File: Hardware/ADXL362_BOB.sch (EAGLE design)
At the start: 9 parts, among them U1 ADXL362

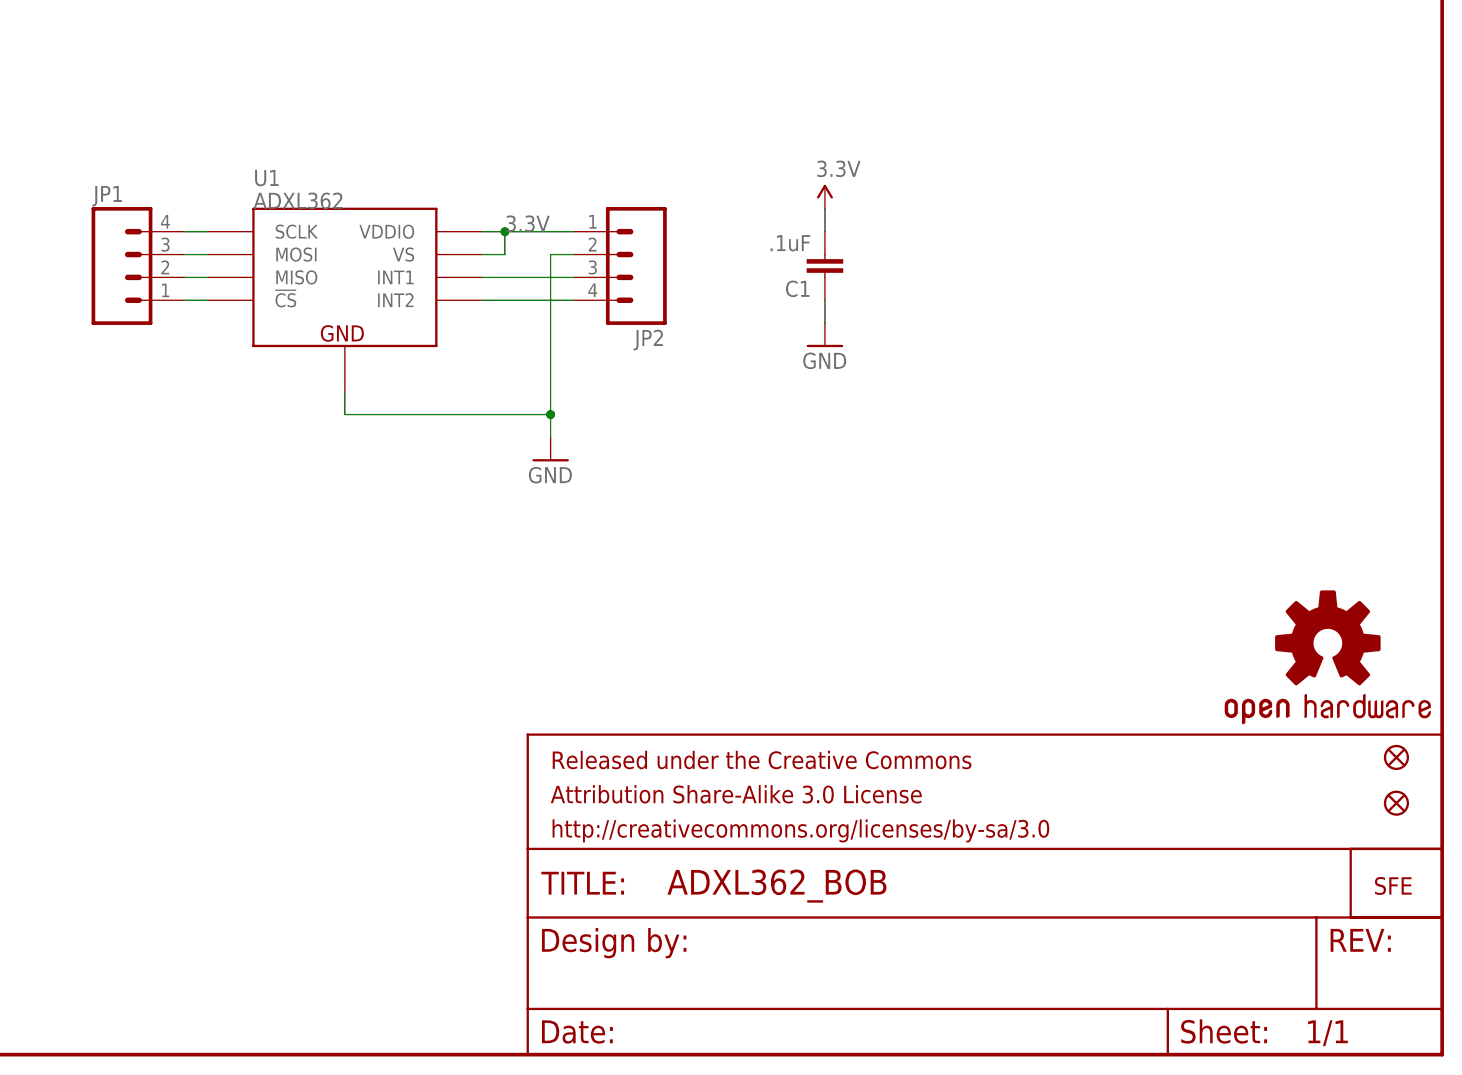
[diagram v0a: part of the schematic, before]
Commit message: Moved to 0603, Traces, 1:1
1:1 on the Adxl362
Minor trace re-route
cap moved to 0603
Sch update
Rev #1 update
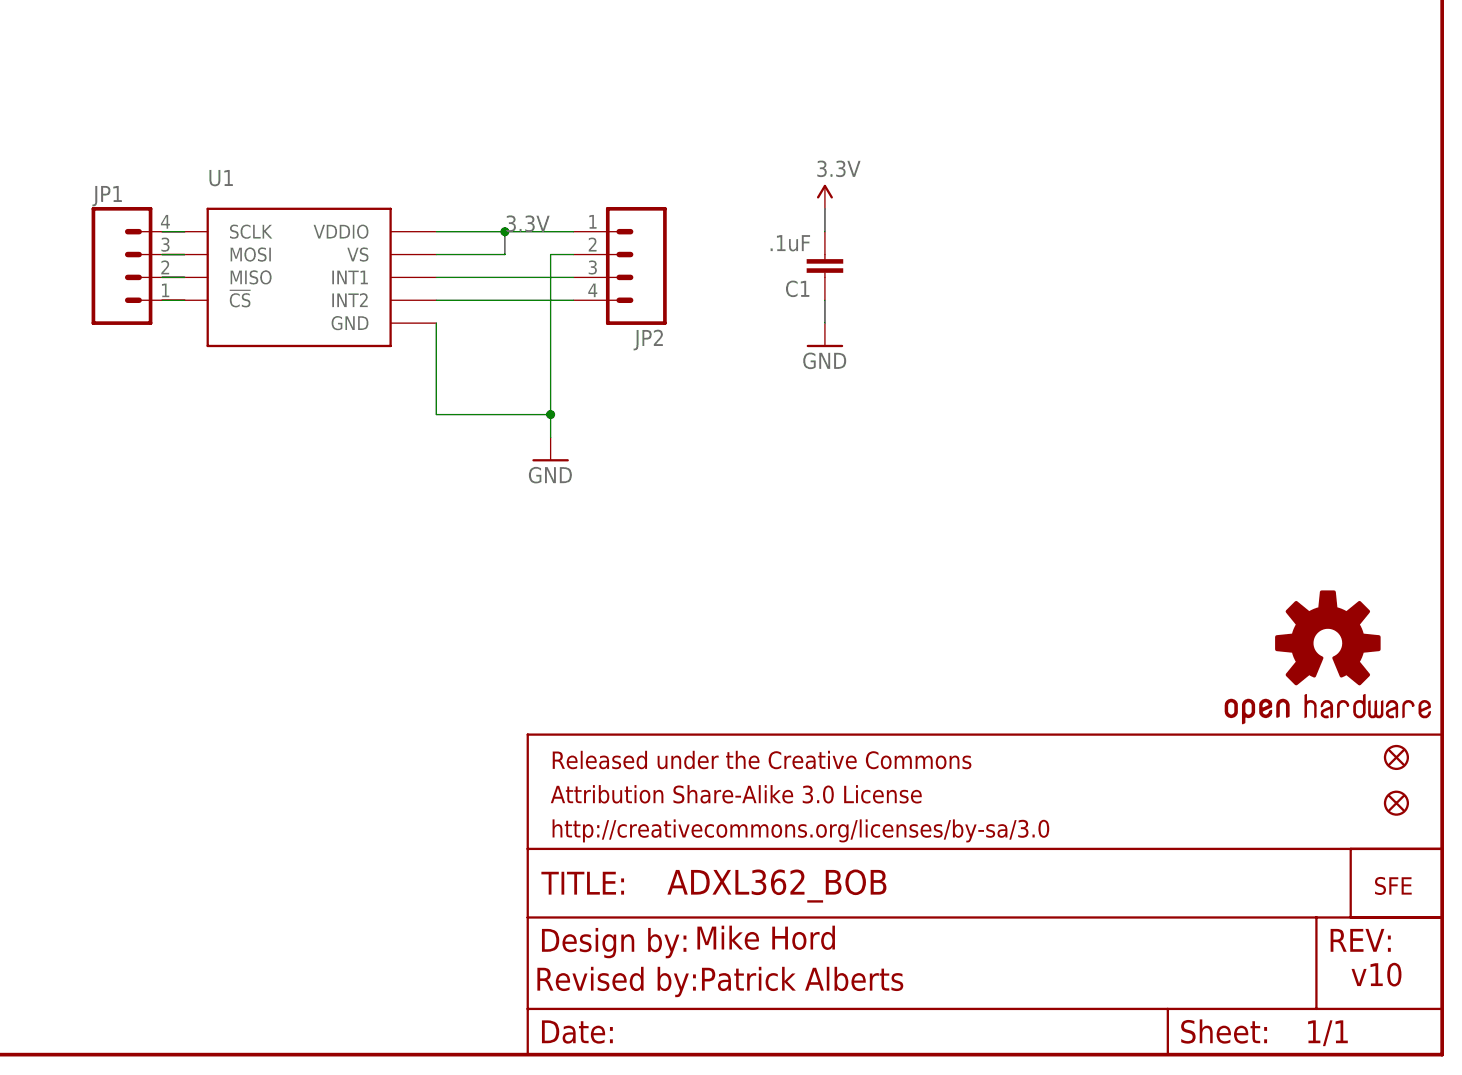
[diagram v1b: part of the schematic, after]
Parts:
- C1: device SparkFun-Passives:CAP0402-CAP -> SparkFun-Capacitors:0.1UF-25V(+80/-20%)(0603)
- U1: value ADXL362 -> (none); device SparkFun-Sensors:ADXL362 -> SparkFun-Sensors:ADXL362ADXL362-1:1
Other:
- note added: "Mike Hord"
- note added: "Revised by:Patrick Alberts"
- note added: "v10"
- moved on the sheet: U1
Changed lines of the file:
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@@
 <?xml version="1.0" encoding="utf-8"?>
 <!DOCTYPE eagle SYSTEM "eagle.dtd">
-<eagle version="6.2">
+<eagle version="6.4">
 <drawing>
 <settings>
@@
 <layer number="106" name="bPlate" color="7" fill="1" visible="no" active="yes"/>
 <layer number="107" name="Crop" color="7" fill="1" visible="no" active="yes"/>
+<layer number="108" name="tplace-old" color="10" fill="1" visible="yes" active="yes"/>
+<layer number="109" name="ref-old" color="11" fill="1" visible="yes" active="yes"/>
 <layer number="116" name="Patch_BOT" color="9" fill="4" visible="no" active="yes"/>
 <layer number="121" name="_tsilk" color="7" fill="1" visible="no" active="yes"/>
@@
 <layer number="144" name="Drill_legend" color="7" fill="1" visible="no" active="yes"/>
 <layer number="151" name="HeatSink" color="7" fill="1" visible="no" active="yes"/>
+<layer number="199" name="Contour" color="7" fill="1" visible="yes" active="yes"/>
 <layer number="200" name="200bmp" color="1" fill="10" visible="no" active="yes"/>
 <layer number="201" name="201bmp" color="2" fill="10" visible="no" active="yes"/>
@@
 </classes>
 <parts>
-<part name="U1" library="SparkFun-Sensors" deviceset="ADXL362" device=""/>
+<part name="U1" library="SparkFun-Sensors" deviceset="ADXL362" device="ADXL362-1:1"/>
 <part name="JP1" library="SparkFun-Connectors" deviceset="M04" device="PTH"/>
 <part name="JP2" library="SparkFun-Connectors" deviceset="M04" device="PTH"/>
-<part name="C1" library="SparkFun-Passives" deviceset="CAP" device="0402-CAP" value=".1uF">
+<part name="C1" library="SparkFun-Capacitors" deviceset="0.1UF-25V(+80/-20%)(0603)" device="" value=".1uF">
 <attribute name="PROD_ID" value="CAP-00810"/>
 </part>
@@
 <sheet>
 <plain>
+<text x="238.76" y="7.62" size="2.54" layer="94">v10</text>
+<text x="165.862" y="11.684" size="2.54" layer="94">Mike Hord</text>
+<text x="148.082" y="7.112" size="2.54" layer="94">Revised by:Patrick Alberts</text>
 </plain>
 <instances>
-<instance part="U1" gate="G$1" x="119.38" y="78.74"/>
+<instance part="U1" gate="G$1" x="121.92" y="86.36"/>
 <instance part="JP1" gate="G$1" x="104.14" y="86.36"/>
 <instance part="JP2" gate="G$1" x="157.48" y="88.9" rot="R180"/>
@@
 <pinref part="JP1" gate="G$1" pin="4"/>
 <pinref part="U1" gate="G$1" pin="SCLK"/>
-<wire x1="109.22" y1="91.44" x2="111.76" y2="91.44" width="0.1524" layer="91"/>
+<wire x1="109.22" y1="91.44" x2="106.68" y2="91.44" width="0.1524" layer="91"/>
 </segment>
 </net>
@@
 <pinref part="U1" gate="G$1" pin="MOSI"/>
 <pinref part="JP1" gate="G$1" pin="3"/>
-<wire x1="111.76" y1="88.9" x2="109.22" y2="88.9" width="0.1524" layer="91"/>
+<wire x1="106.68" y1="88.9" x2="109.22" y2="88.9" width="0.1524" layer="91"/>
 </segment>
 </net>
@@
 <pinref part="JP1" gate="G$1" pin="2"/>
 <pinref part="U1" gate="G$1" pin="MISO"/>
-<wire x1="109.22" y1="86.36" x2="111.76" y2="86.36" width="0.1524" layer="91"/>
+<wire x1="109.22" y1="86.36" x2="106.68" y2="86.36" width="0.1524" layer="91"/>
 </segment>
 </net>
@@
 <pinref part="U1" gate="G$1" pin="!CS"/>
 <pinref part="JP1" gate="G$1" pin="1"/>
-<wire x1="111.76" y1="83.82" x2="109.22" y2="83.82" width="0.1524" layer="91"/>
+<wire x1="106.68" y1="83.82" x2="109.22" y2="83.82" width="0.1524" layer="91"/>
 </segment>
 </net>
@@
 <wire x1="152.4" y1="91.44" x2="144.78" y2="91.44" width="0.1524" layer="91"/>
 <pinref part="U1" gate="G$1" pin="VS"/>
-<wire x1="144.78" y1="91.44" x2="142.24" y2="91.44" width="0.1524" layer="91"/>
-<wire x1="142.24" y1="88.9" x2="144.78" y2="88.9" width="0.1524" layer="91"/>
+<wire x1="144.78" y1="91.44" x2="137.16" y2="91.44" width="0.1524" layer="91"/>
+<wire x1="137.16" y1="88.9" x2="144.78" y2="88.9" width="0.1524" layer="91"/>
 <wire x1="144.78" y1="88.9" x2="144.78" y2="91.44" width="0.1524" layer="91"/>
 <junction x="144.78" y="91.44"/>
@@
 <pinref part="U1" gate="G$1" pin="INT1"/>
 <pinref part="JP2" gate="G$1" pin="3"/>
-<wire x1="152.4" y1="86.36" x2="142.24" y2="86.36" width="0.1524" layer="91"/>
+<wire x1="152.4" y1="86.36" x2="137.16" y2="86.36" width="0.1524" layer="91"/>
 </segment>
 </net>
@@
 <pinref part="U1" gate="G$1" pin="INT2"/>
 <pinref part="JP2" gate="G$1" pin="4"/>
-<wire x1="152.4" y1="83.82" x2="142.24" y2="83.82" width="0.1524" layer="91"/>
+<wire x1="152.4" y1="83.82" x2="137.16" y2="83.82" width="0.1524" layer="91"/>
 </segment>
 </net>
@@
 <segment>
 <pinref part="U1" gate="G$1" pin="GND"/>
-<wire x1="127" y1="73.66" x2="127" y2="71.12" width="0.1524" layer="91"/>
-<wire x1="127" y1="71.12" x2="149.86" y2="71.12" width="0.1524" layer="91"/>
+<wire x1="137.16" y1="81.28" x2="137.16" y2="71.12" width="0.1524" layer="91"/>
+<wire x1="137.16" y1="71.12" x2="149.86" y2="71.12" width="0.1524" layer="91"/>
 <wire x1="149.86" y1="71.12" x2="149.86" y2="88.9" width="0.1524" layer="91"/>
 <pinref part="JP2" gate="G$1" pin="2"/>

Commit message: changed fiducials from micro to regular
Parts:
- removed JP4, JP5: FIDUCIALUFIDUCIAL, SparkFun:FIDUCIALUFIDUCIAL
- added FID1, FID2: FIDUCIAL1X2, SparkFun-Aesthetics:FIDUCIAL1X2
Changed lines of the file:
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@@
 <?xml version="1.0" encoding="utf-8"?>
 <!DOCTYPE eagle SYSTEM "eagle.dtd">
-<eagle version="6.4">
+<eagle version="6.5.0">
 <drawing>
 <settings>
@@
 <part name="FRAME1" library="SparkFun-Aesthetics" deviceset="FRAME-LETTER" device=""/>
 <part name="GND2" library="SparkFun-Aesthetics" deviceset="GND" device=""/>
-<part name="JP4" library="SparkFun" deviceset="FIDUCIAL" device="UFIDUCIAL"/>
-<part name="JP5" library="SparkFun" deviceset="FIDUCIAL" device="UFIDUCIAL"/>
+<part name="FID1" library="SparkFun-Aesthetics" deviceset="FIDUCIAL" device="1X2"/>
+<part name="FID2" library="SparkFun-Aesthetics" deviceset="FIDUCIAL" device="1X2"/>
 </parts>
 <sheets>
@@
 <instance part="FRAME1" gate="G$2" x="147.32" y="0"/>
 <instance part="GND2" gate="1" x="149.86" y="66.04"/>
-<instance part="JP4" gate="G$1" x="243.84" y="33.02"/>
-<instance part="JP5" gate="G$1" x="243.84" y="27.94"/>
+<instance part="FID1" gate="G$1" x="238.76" y="33.02"/>
+<instance part="FID2" gate="G$1" x="238.76" y="27.94"/>
 </instances>
 <busses>
